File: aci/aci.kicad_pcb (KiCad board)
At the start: 2 copper layers, 102.2 x 53.3 mm, 19 parts, among them Q1 Q_NPN_EBC, Q2 Q_NPN_EBC

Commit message: additional footprint work
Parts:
- A1: footprint Package_DIP:DIP-8_W7.62mm -> aci:apple-1_DIP-8_W7.62mm
- A2, A5, A6: footprint Package_DIP:DIP-14_W7.62mm -> aci:apple-1_DIP-14_W7.62mm
- A3, A4: footprint Package_DIP:DIP-16_W7.62mm -> aci:apple-1_DIP-16_W7.62mm
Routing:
- net (no net): track 4121.1 -> 4115.9 mm, vias 6 -> 0
- net Net-(A4-O2): track 241.3 -> 241.0 mm, vias 1 -> 0
- net Net-(A4-O4): track 248.0 -> 248.4 mm, vias 1 -> 0
- net Net-(A3-O4): track 254.8 -> 255.1 mm, vias 1 -> 0
- net Net-(A3-A2): track 270.9 -> 271.2 mm, vias 2 -> 0
- net Net-(J3A-A9): track 237.3 -> 237.1 mm, vias 2 -> 1
- net Net-(A3-O2): track 246.2 -> 246.0 mm, vias 1 -> 0
- net Net-(A4-O1): track 238.3 -> 238.1 mm, vias 2 -> 1
- net Net-(J3A-A11): track 259.8 -> 260.0 mm, vias 2 -> 1
- net Net-(A3-A3): track 303.6 -> 303.4 mm, vias 3 -> 1
- net Net-(A3-O1): track 245.2 -> 245.1 mm, vias 2 -> 1
- net Net-(A3-O3): track 250.9 -> 250.8 mm, vias 2 -> 1
- net Net-(J3A-~{4KCS}): vias 2 -> 1
- net Net-(A4-O3): vias 2 -> 1
- net Net-(A3-A7): vias 4 -> 1
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
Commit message: completed aci, added p-l4b boards
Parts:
- added C1: 0.01u, aci:C_Disc_.01_p350MILS, F.Cu at (37.5, -55.2)
- added J1: Switchcraft #41, aci:aci_phonopads_frmtape, F.Cu at (16.5, -43.8)
- added J2: Switchcraft #41, aci:aci_phonopads, F.Cu at (16.5, -55.2)
- added J3: ACI_EdgeConnector, aci:aci_edgecon, F.Cu at (25.4, -19.7)
- R1, R10, R2, R3, R4, R5, R6, R7, R8, R9: footprint Resistor_THT:R_Axial_DIN0207_L6.3mm_D2.5mm_P10.16mm_Horizontal -> aci:R_Axial_ACI
- moved A3 14.0 mm to (64.1, -31.1)
- moved A4 14.0 mm to (78.1, -31.1)
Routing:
- net (no net): track 4115.9 -> 108.1 mm
- net Net-(A3-O1): track 245.1 -> 27.5 mm
- net Net-(A3-O3): track 250.8 -> 34.3 mm
- net Net-(A3-O4): track 255.1 -> 42.5 mm
- net Net-(A3-O2): track 246.0 -> 35.2 mm
- net Net-(J3A-A9): track 237.1 -> 26.3 mm
- net Net-(J3A-A11): track 260.0 -> 49.2 mm
- net GND: track 458.4 -> 248.1 mm, vias 4 -> 1
- net Net-(A3-A7): track 289.1 -> 78.8 mm
- net Net-(A3-A4): track 262.3 -> 52.1 mm
- net Net-(J3A-~{4KCS}): track 236.6 -> 26.4 mm
- net Net-(J3A-ɸ2): track 332.7 -> 122.6 mm
- net Net-(A3-A6): track 254.4 -> 44.4 mm
- net Net-(J3A-A8): track 232.8 -> 24.5 mm
- net Net-(J3A-A10): track 240.4 -> 34.6 mm
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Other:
- outline, holes or cut-outs redrawn
- board text added: "FRM TAPE"
- board text added: "TO TAPE"

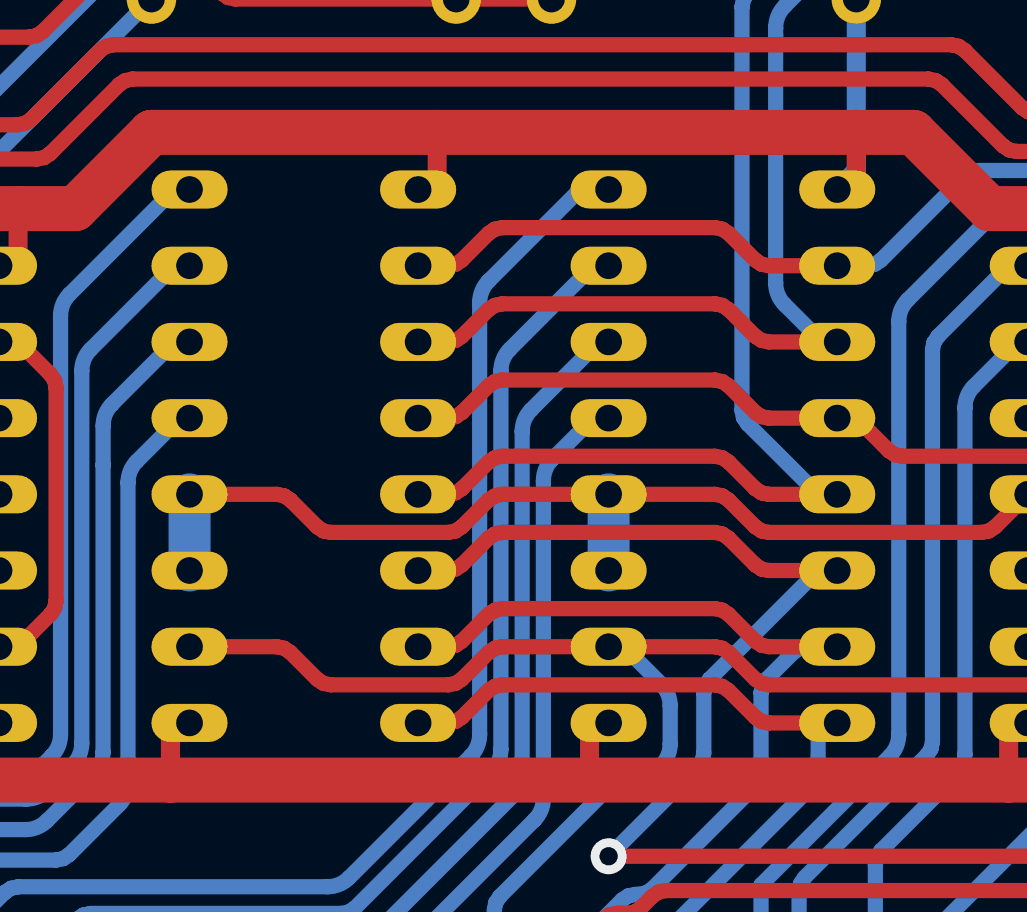
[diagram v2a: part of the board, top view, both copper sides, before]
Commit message: merged /transformers with /mainboard
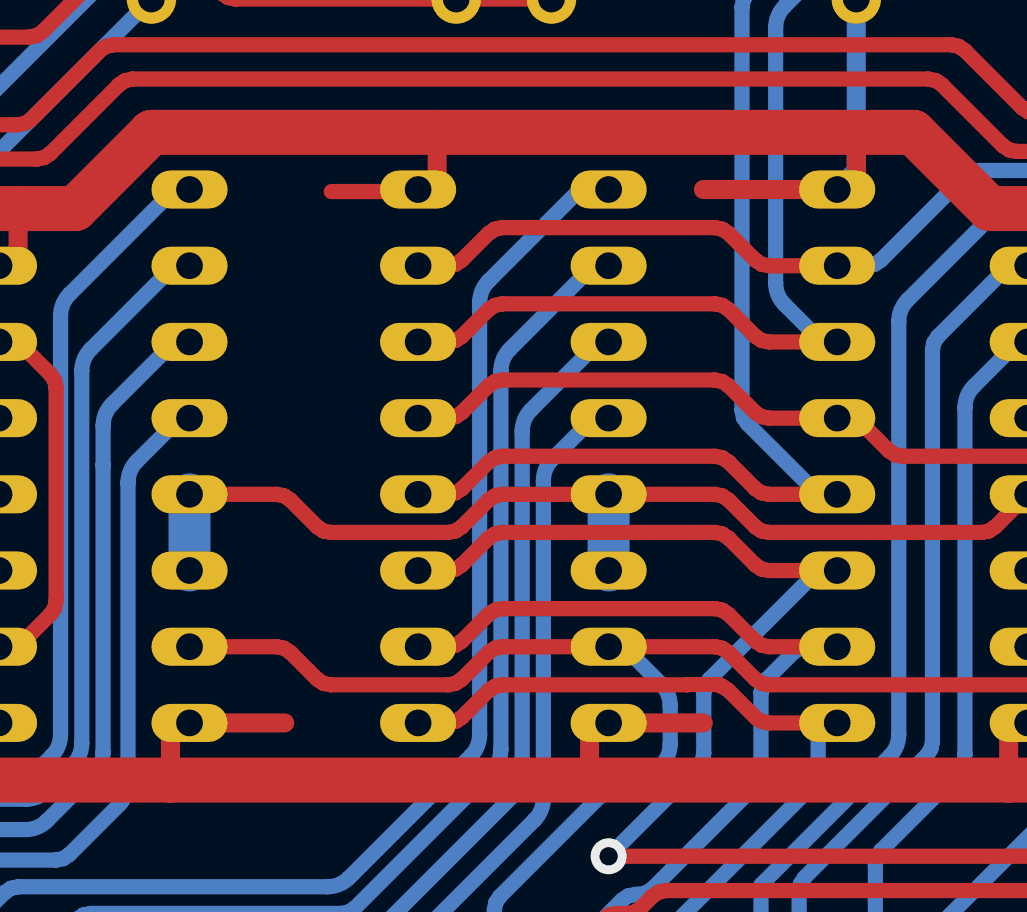
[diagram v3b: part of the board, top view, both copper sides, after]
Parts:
- C1: value 0.01u -> 0.01UF
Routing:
- net GND: track 248.1 -> 255.5 mm
- net +5V: track 157.0 -> 163.3 mm
